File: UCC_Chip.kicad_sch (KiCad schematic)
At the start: 11 parts, among them U2 UCC28710DR

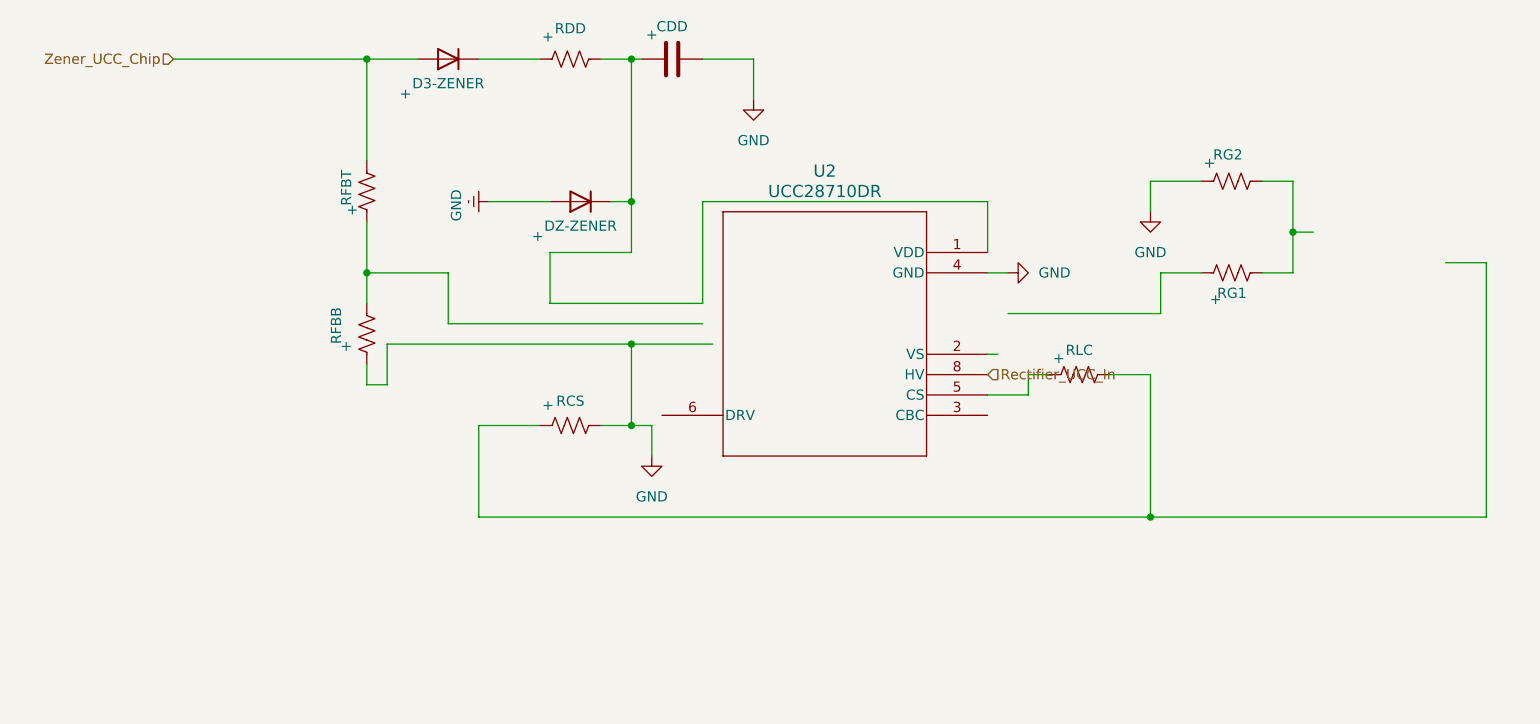
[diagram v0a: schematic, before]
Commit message: Mosfet&UCC
Added Mosfet with label and rewired the UCC chip
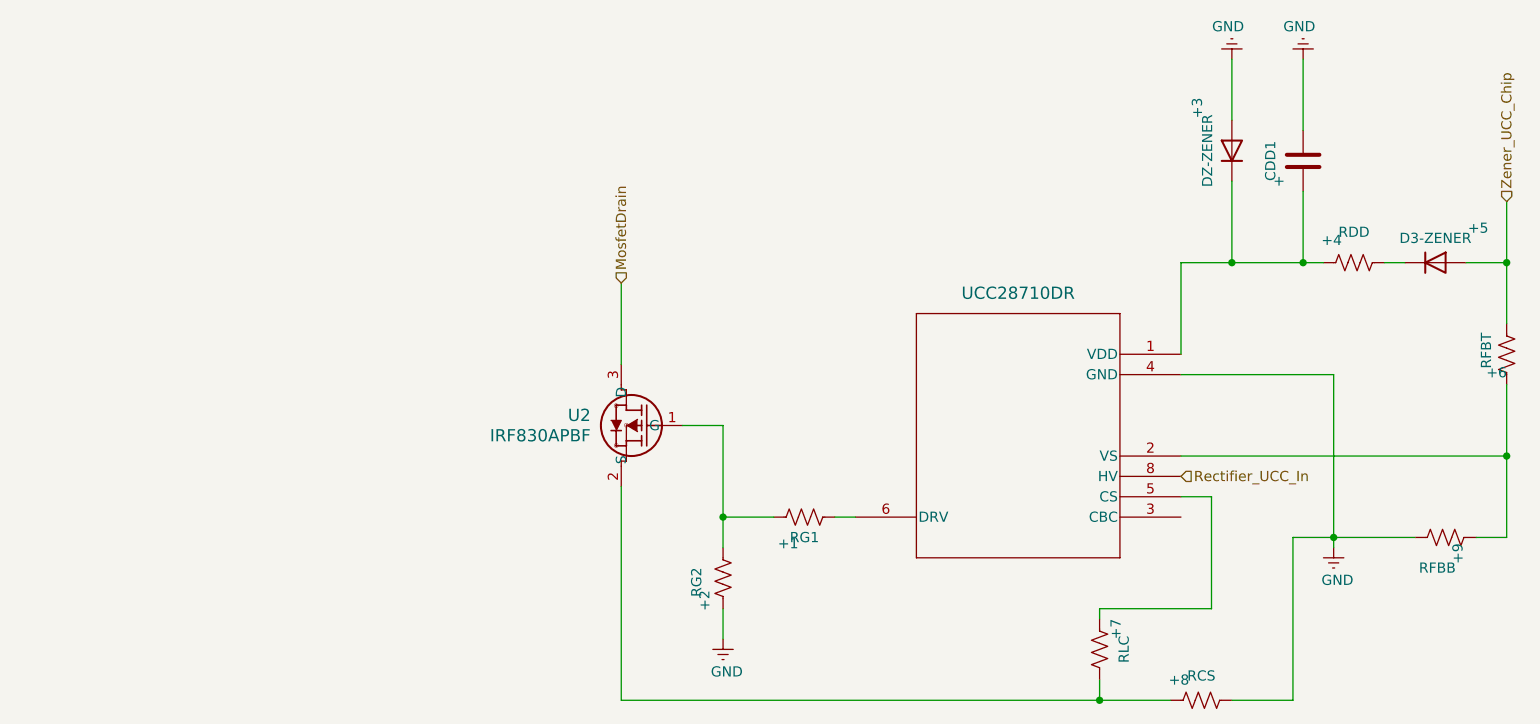
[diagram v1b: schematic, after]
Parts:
- removed +: RCS, symbol Device:R_US
- removed +: RDD, symbol Device:R_US
- removed +: RFBB, symbol Device:R_US
- removed +: D3-ZENER, Diode_THT:D_DO-35_SOD27_P7.62mm_Horizontal, symbol Diode:1N914
- removed +: DZ-ZENER, Diode_THT:D_DO-35_SOD27_P7.62mm_Horizontal, symbol Diode:1N914
- removed +: RLC, symbol Device:R_US
- removed +: RG1, symbol Device:R_US
- removed +: RG2, symbol Device:R_US
- removed +: RFBT, symbol Device:R_US
- removed CDD: +, Package_SO:SOIC-8_3.9x4.9mm_P1.27mm, symbol Device:C
- removed U2: UCC28710DR, SO_UCC28710D_TEX, symbol UCCfixed:UCC28710DR
- added +1: RG1, symbol Device:R_US
- added +2: RG2, symbol Device:R_US
- added +3: DZ-ZENER, Diode_THT:D_DO-35_SOD27_P7.62mm_Horizontal, symbol Diode:1N914
- added +4: RDD, symbol Device:R_US
- added +5: D3-ZENER, Diode_THT:D_DO-35_SOD27_P7.62mm_Horizontal, symbol Diode:1N914
- added +6: RFBT, symbol Device:R_US
- added +7: RLC, symbol Device:R_US
- added +8: RCS, symbol Device:R_US
- added +9: RFBB, symbol Device:R_US
- added CDD1: +, Package_SO:SOIC-8_3.9x4.9mm_P1.27mm, symbol Device:C
- added U2: IRF830APBF, TO220AB_VIS, symbol 2026-10-04_19-09-28:IRF830APBF
- added U3: UCC28710DR, SO_UCC28710D_TEX, symbol UCCfixed:UCC28710DR
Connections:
- net GND: now also +2.1, +3.2 (A), +8.2, +9.1, CDD1.2, U3.4 (GND)
- net Rectifier_UCC_In: now also U3.8 (HV)
- net Zener_UCC_Chip: now also +5.2 (A), +6.1
- new net: +4.2, +5.1 (K)
- new net: +7.2, +8.1, U2.2 (S)
- new net: +1.1, +2.2, U2.1 (G)
- new net: +3.1 (K), +4.1, CDD1.1, U3.1 (VDD)
- new net: +1.2, U3.6 (DRV)
- new net: +6.2, +9.2, U3.2 (VS)
- new net: +7.1, U3.5 (CS)
- new net MosfetDrain: U2.3 (D)

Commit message: FootprintUpdate
Now UCC has footprints
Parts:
- +1, +2, +4, +6, +7, +8, +9: footprint (none) -> Resistor_THT:R_Axial_DIN0207_L6.3mm_D2.5mm_P10.16mm_Horizontal
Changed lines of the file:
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@@
 			)
 		)
-		(property "Footprint" ""
+		(property "Footprint" "Resistor_THT:R_Axial_DIN0207_L6.3mm_D2.5mm_P10.16mm_Horizontal"
 			(at 159.004 132.334 90)
 			(hide yes)
@@
 			)
 		)
-		(property "Footprint" ""
+		(property "Footprint" "Resistor_THT:R_Axial_DIN0207_L6.3mm_D2.5mm_P10.16mm_Horizontal"
 			(at 178.054 77.724 90)
 			(hide yes)
@@
 			)
 		)
-		(property "Footprint" ""
+		(property "Footprint" "Resistor_THT:R_Axial_DIN0207_L6.3mm_D2.5mm_P10.16mm_Horizontal"
 			(at 109.474 109.474 90)
 			(hide yes)
@@
 			)
 		)
-		(property "Footprint" ""
+		(property "Footprint" "Resistor_THT:R_Axial_DIN0207_L6.3mm_D2.5mm_P10.16mm_Horizontal"
 			(at 189.484 112.014 90)
 			(hide yes)
@@
 			)
 		)
-		(property "Footprint" ""
+		(property "Footprint" "Resistor_THT:R_Axial_DIN0207_L6.3mm_D2.5mm_P10.16mm_Horizontal"
 			(at 197.866 90.424 90)
 			(hide yes)
@@
 			)
 		)
-		(property "Footprint" ""
+		(property "Footprint" "Resistor_THT:R_Axial_DIN0207_L6.3mm_D2.5mm_P10.16mm_Horizontal"
 			(at 98.044 117.856 90)
 			(hide yes)
@@
 			)
 		)
-		(property "Footprint" ""
+		(property "Footprint" "Resistor_THT:R_Axial_DIN0207_L6.3mm_D2.5mm_P10.16mm_Horizontal"
 			(at 147.066 127.254 90)
 			(hide yes)

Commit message: FixedMostIssues
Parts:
- renumbered +3 to +10, +4 to +11, +5 to +12, +9 to +13, +6 to +14, +2 to +6, +1 to +7, +7 to +8, +8 to +9
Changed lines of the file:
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@@
 		(in_pos_files yes)
 		(dnp no)
-		(property "Reference" "+5"
+		(property "Reference" "+12"
 			(at 193.294 74.422 0)
 			(show_name no)
@@
 			(project "Solar_Battery"
 				(path "/6805959e-39bb-4644-b93e-3970e29fedc0/a320594e-eb17-43a9-8193-2f75b3718179/23661c41-dbb5-4ca2-a742-531e78ada01c"
-					(reference "+5")
+					(reference "+12")
 					(unit 1)
 				)
@@
 		(in_pos_files yes)
 		(dnp no)
-		(property "Reference" "+8"
+		(property "Reference" "+9"
 			(at 155.956 130.81 90)
 			(show_name no)
@@
 			(project "Solar_Battery"
 				(path "/6805959e-39bb-4644-b93e-3970e29fedc0/a320594e-eb17-43a9-8193-2f75b3718179/23661c41-dbb5-4ca2-a742-531e78ada01c"
-					(reference "+8")
+					(reference "+9")
 					(unit 1)
 				)
@@
 		(in_pos_files yes)
 		(dnp no)
-		(property "Reference" "#PWR018"
+		(property "Reference" "#PWR019"
 			(at 175.26 120.65 0)
 			(hide yes)
@@
 			(project "Solar_Battery"
 				(path "/6805959e-39bb-4644-b93e-3970e29fedc0/a320594e-eb17-43a9-8193-2f75b3718179/23661c41-dbb5-4ca2-a742-531e78ada01c"
-					(reference "#PWR018")
+					(reference "#PWR019")
 					(unit 1)
 				)
@@
 		(in_pos_files yes)
 		(dnp no)
-		(property "Reference" "#PWR017"
+		(property "Reference" "#PWR018"
 			(at 171.45 46.99 0)
 			(hide yes)
@@
 			(project "Solar_Battery"
 				(path "/6805959e-39bb-4644-b93e-3970e29fedc0/a320594e-eb17-43a9-8193-2f75b3718179/23661c41-dbb5-4ca2-a742-531e78ada01c"
-					(reference "#PWR017")
+					(reference "#PWR018")
 					(unit 1)
 				)
@@
 		(in_pos_files yes)
 		(dnp no)
-		(property "Reference" "+4"
+		(property "Reference" "+11"
 			(at 175.006 75.946 90)
 			(show_name no)
@@
 			(project "Solar_Battery"
 				(path "/6805959e-39bb-4644-b93e-3970e29fedc0/a320594e-eb17-43a9-8193-2f75b3718179/23661c41-dbb5-4ca2-a742-531e78ada01c"
-					(reference "+4")
+					(reference "+11")
 					(unit 1)
 				)
@@
 		(in_pos_files yes)
 		(dnp no)
-		(property "Reference" "#PWR05"
+		(property "Reference" "#PWR017"
 			(at 162.56 46.99 0)
 			(hide yes)
@@
 			(project "Solar_Battery"
 				(path "/6805959e-39bb-4644-b93e-3970e29fedc0/a320594e-eb17-43a9-8193-2f75b3718179/23661c41-dbb5-4ca2-a742-531e78ada01c"
-					(reference "#PWR05")
+					(reference "#PWR017")
 					(unit 1)
 				)
@@
 		(in_pos_files yes)
 		(dnp no)
-		(property "Reference" "+1"
+		(property "Reference" "+7"
 			(at 107.188 113.792 90)
 			(show_name no)
@@
 			(project "Solar_Battery"
 				(path "/6805959e-39bb-4644-b93e-3970e29fedc0/a320594e-eb17-43a9-8193-2f75b3718179/23661c41-dbb5-4ca2-a742-531e78ada01c"
-					(reference "+1")
+					(reference "+7")
 					(unit 1)
 				)
@@
 		(in_pos_files yes)
 		(dnp no)
-		(property "Reference" "+9"
+		(property "Reference" "+13"
 			(at 190.754 116.332 0)
 			(show_name no)
@@
 			(project "Solar_Battery"
 				(path "/6805959e-39bb-4644-b93e-3970e29fedc0/a320594e-eb17-43a9-8193-2f75b3718179/23661c41-dbb5-4ca2-a742-531e78ada01c"
-					(reference "+9")
+					(reference "+13")
 					(unit 1)
 				)
@@
 		(in_pos_files yes)
 		(dnp no)
-		(property "Reference" "+6"
+		(property "Reference" "+14"
 			(at 194.31 92.456 0)
 			(show_name no)
@@
 			(project "Solar_Battery"
 				(path "/6805959e-39bb-4644-b93e-3970e29fedc0/a320594e-eb17-43a9-8193-2f75b3718179/23661c41-dbb5-4ca2-a742-531e78ada01c"
-					(reference "+6")
+					(reference "+14")
 					(unit 1)
 				)
@@
 		(in_pos_files yes)
 		(dnp no)
-		(property "Reference" "+3"
+		(property "Reference" "+10"
 			(at 158.242 59.436 0)
 			(show_name no)
@@
 			(project "Solar_Battery"
 				(path "/6805959e-39bb-4644-b93e-3970e29fedc0/a320594e-eb17-43a9-8193-2f75b3718179/23661c41-dbb5-4ca2-a742-531e78ada01c"
-					(reference "+3")
+					(reference "+10")
 					(unit 1)
 				)
@@
 		(in_pos_files yes)
 		(dnp no)
-		(property "Reference" "+2"
+		(property "Reference" "+6"
 			(at 96.774 120.904 90)
 			(show_name no)
@@
 			(project "Solar_Battery"
 				(path "/6805959e-39bb-4644-b93e-3970e29fedc0/a320594e-eb17-43a9-8193-2f75b3718179/23661c41-dbb5-4ca2-a742-531e78ada01c"
-					(reference "+2")
+					(reference "+6")
 					(unit 1)
 				)
@@
 		(in_pos_files yes)
 		(dnp no)
-		(property "Reference" "#PWR015"
+		(property "Reference" "#PWR016"
 			(at 99.06 132.08 0)
 			(hide yes)
@@
 			(project "Solar_Battery"
 				(path "/6805959e-39bb-4644-b93e-3970e29fedc0/a320594e-eb17-43a9-8193-2f75b3718179/23661c41-dbb5-4ca2-a742-531e78ada01c"
-					(reference "#PWR015")
+					(reference "#PWR016")
 					(unit 1)
 				)
@@
 		(in_pos_files yes)
 		(dnp no)
-		(property "Reference" "+7"
+		(property "Reference" "+8"
 			(at 148.082 124.46 90)
 			(show_name no)
@@
 			(project "Solar_Battery"
 				(path "/6805959e-39bb-4644-b93e-3970e29fedc0/a320594e-eb17-43a9-8193-2f75b3718179/23661c41-dbb5-4ca2-a742-531e78ada01c"
-					(reference "+7")
-					(unit 1)
-				)
+					(reference "+8")
+					(unit 1)
+				)

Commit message: PCB setup for next meeting
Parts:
- U2: footprint TO220AB_VIS -> footprints:TO220AB_VIS
- U3: footprint SO_UCC28710D_TEX -> footprints:SO_UCC28710D_TEX
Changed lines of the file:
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@@
 			)
 		)
-		(property "Footprint" "TO220AB_VIS"
+		(property "Footprint" "footprints:TO220AB_VIS"
 			(at 93.98 99.06 0)
 			(hide yes)
@@
 			)
 		)
-		(property "Footprint" "SO_UCC28710D_TEX"
+		(property "Footprint" "footprints:SO_UCC28710D_TEX"
 			(at 156.21 110.49 0)
 			(hide yes)
